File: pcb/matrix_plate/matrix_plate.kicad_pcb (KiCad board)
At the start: 2 copper layers, 269.2 x 122.9 mm, 73 parts

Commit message: Continue re-routing matrix plate to move diodes to front.
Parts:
- moved R_R_A1 7.63 mm to (256.0, 42.0)
- moved R_R_A2 7.63 mm to (256.0, 44.5)
- moved R_L_SCL_1 6.52 mm to (46.0, 37.0)
- moved R_R_SCL_1 6.52 mm to (260.5, 39.5), turned to 0 degrees
- moved R_R_SDA_1 6.52 mm to (260.5, 37.0), turned to 180 degrees
- moved R_L_A0 5.50 mm to (42.0, 44.5), turned to 0 degrees
- moved R_L_A1 5.50 mm to (42.0, 42.0), turned to 180 degrees
- moved R_L_A2 5.50 mm to (42.0, 39.5), turned to 180 degrees
- moved R_R_A0 4.27 mm to (256.0, 39.5)
- moved R_R_RST_1 4.27 mm to (256.0, 37.0)
- moved R_L_SDA_1 4.00 mm to (46.0, 39.5)
- moved R_L_RST_1 0.15 mm to (42.0, 37.0), turned to 180 degrees
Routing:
- net /Right/R3: track 50.9 -> 245.9 mm, vias 0 -> 1
- net /Right/CHG_STAT: track 0.00 -> 194.6 mm, vias 0 -> 2
- net /Left/SDA: track 0.00 -> 190.4 mm
- net /Left/SCL: track 0.00 -> 189.6 mm
- net /Right/C5: track 1.60 -> 186.2 mm, vias 1 -> 0
- net /Right/R2: track 61.0 -> 230.2 mm, vias 0 -> 1
- net /Right/R1: track 61.0 -> 225.8 mm, vias 0 -> 1
- net /Left/C5: track 39.9 -> 204.2 mm, vias 1 -> 0
- net /Right/C4: track 1.64 -> 143.8 mm, vias 1 -> 0
- net /Right/C3: track 1.52 -> 129.4 mm, vias 1 -> 0
- net /Left/C4: track 60.4 -> 164.9 mm, vias 1 -> 0
- net /Right/C2: track 1.62 -> 99.4 mm, vias 1 -> 0
- net /Left/R3: track 144.2 -> 240.4 mm, vias 0 -> 1
- net /Right/C0: track 1.00 -> 95.4 mm, vias 1 -> 0
- net /Right/R0: track 51.3 -> 139.0 mm, vias 0 -> 1
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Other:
- outline, holes or cut-outs redrawn

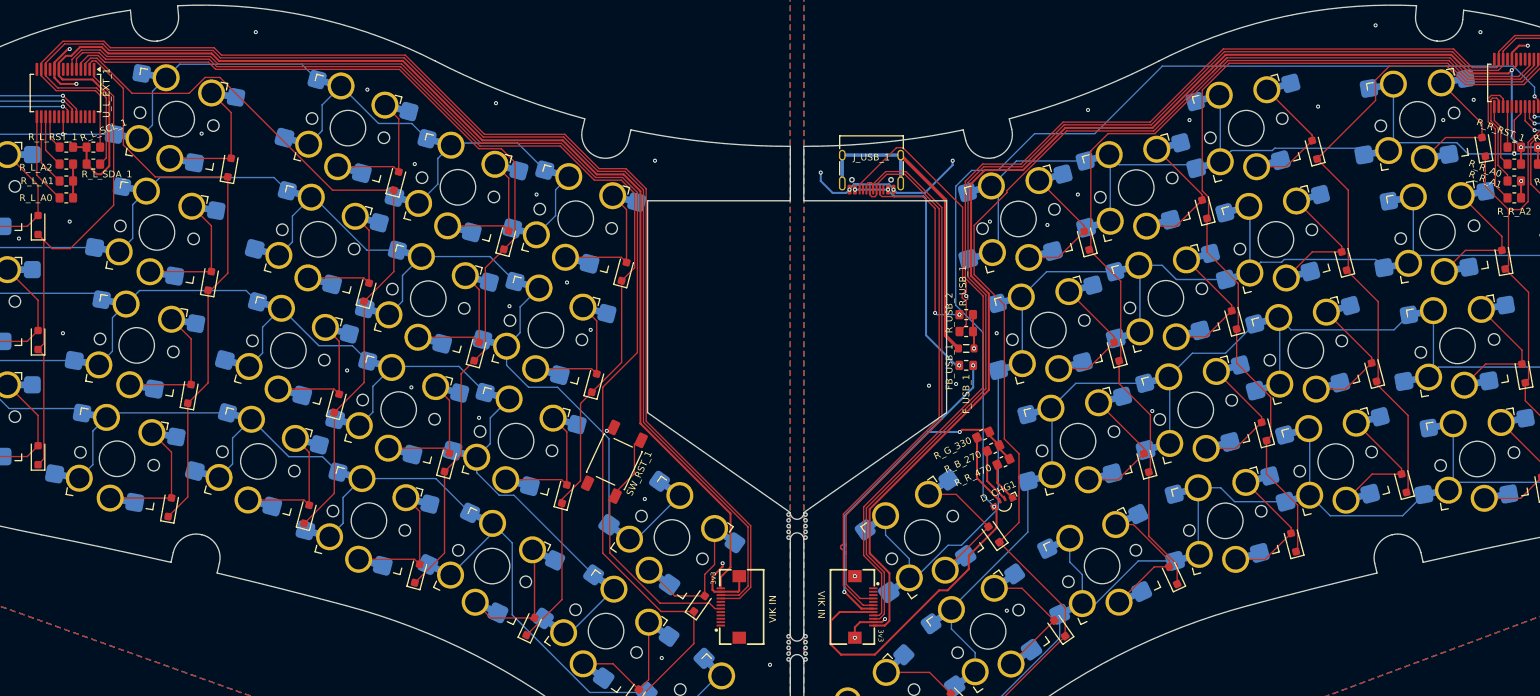
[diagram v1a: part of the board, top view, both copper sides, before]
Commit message: Finish re-routing matrix PCB.
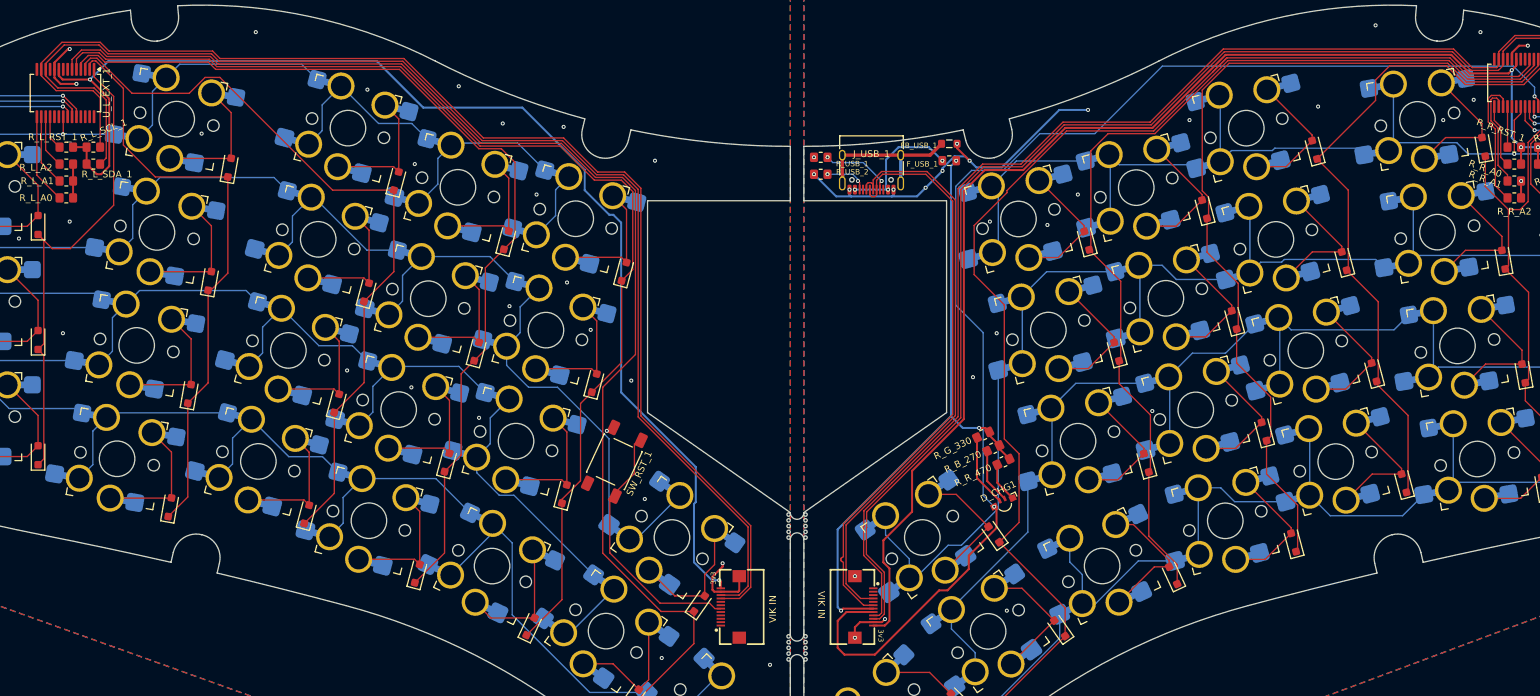
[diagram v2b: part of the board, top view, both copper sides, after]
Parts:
- moved R_USB_1 31.7 mm to (153.5, 38.5), turned to 180 degrees
- moved R_USB_2 31.7 mm to (153.5, 41.0), turned to 180 degrees
- moved FB_USB_1 30.4 mm to (172.5, 36.5)
- moved F_USB_1 30.4 mm to (172.5, 39.0)
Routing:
- net Net-(J_USB_1-CC2): track 41.7 -> 6.43 mm, vias 0 -> 2
- net /Right/VUSB: track 61.2 -> 90.7 mm
- net /Right/SH: track 49.1 -> 23.7 mm
- net /Right/GND: track 42.8 -> 66.4 mm, vias 32 -> 33
- net /Right/VUSB_RAW: track 38.1 -> 19.4 mm
- net Net-(J_USB_1-CC1): track 28.9 -> 10.8 mm
- net /Left/VDD: track 190.4 -> 181.0 mm, vias 0 -> 2
- net /Right/VDD: track 187.4 -> 183.5 mm
- net /Right/D+: track 83.1 -> 86.9 mm
- net /Right/D-: track 83.1 -> 86.9 mm
- net /Right/SDA: track 190.3 -> 188.2 mm
- net /Right/SCL: track 193.6 -> 191.4 mm
- net /Right/CHG_STAT: track 194.6 -> 193.3 mm
- net /Left/SDA: track 190.4 -> 189.6 mm
- net /Left/SCL: track 189.6 -> 188.9 mm
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
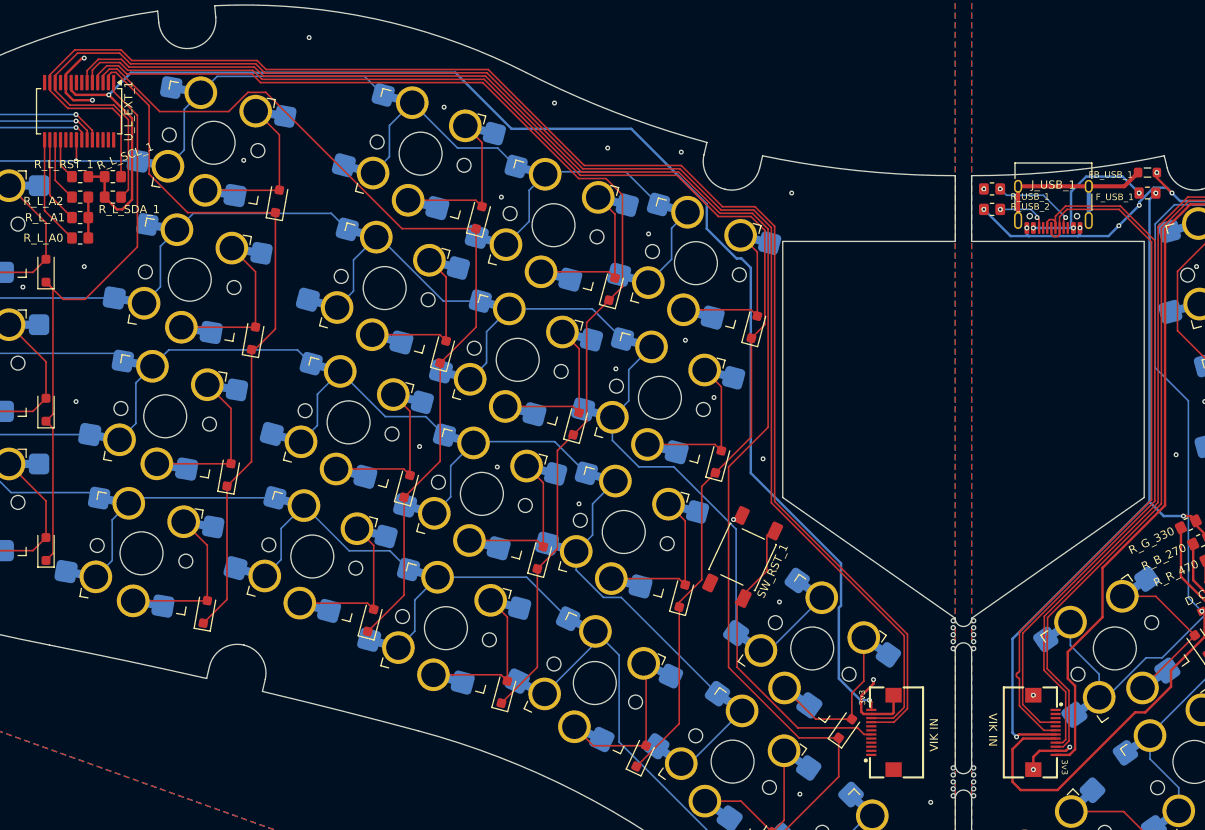
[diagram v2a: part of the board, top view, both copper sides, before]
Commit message: Update KiCAD projects to use new library locations.
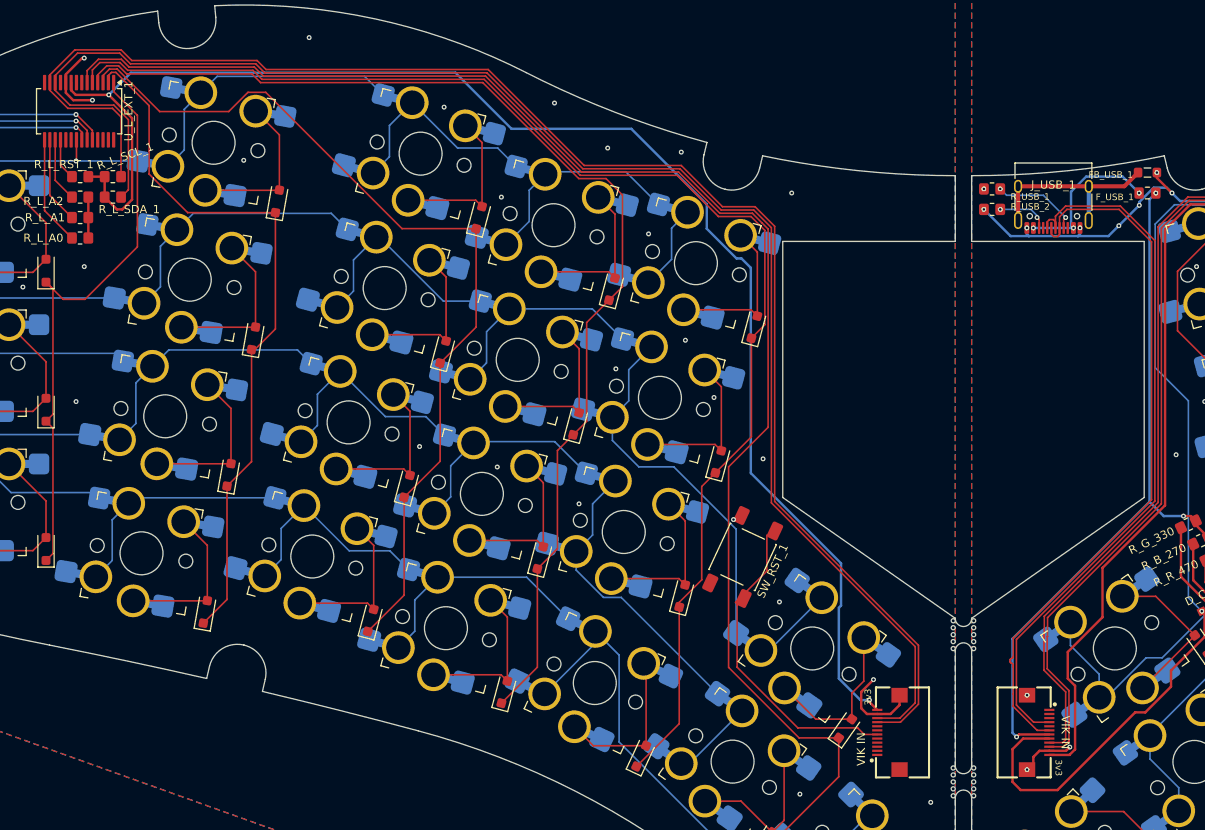
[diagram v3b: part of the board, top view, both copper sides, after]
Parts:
- J_L_VIK_1, J_R_VIK_1: footprint vik:vik-module-connector-horizontal -> footprints:vik-module-connector-horizontal
- S_L_00, S_L_01, S_L_02, S_L_03, S_L_04, S_L_10, S_L_11, S_L_12, S_L_13, S_L_14, S_L_15, S_L_20, S_L_21, S_L_22, S_L_23, S_L_24, S_L_25, S_L_31, S_L_32, S_L_33, S_L_34, S_L_35, S_R_00, S_R_01, S_R_02, S_R_03, S_R_04, S_R_10, S_R_11, S_R_12, S_R_13, S_R_14, S_R_15, S_R_20, S_R_21, S_R_22, S_R_23, S_R_24, S_R_25, S_R_31, S_R_32, S_R_33, S_R_34, S_R_35: footprint key-switches:SW_GLP_Kailh_Choc_V1V2_HotSwap_PTH -> footprints:SW_GLP_Kailh_Choc_V1V2_HotSwap_PTH
- moved J_R_VIK_1 0.77 mm to (158.5, 105.0)
- moved J_L_VIK_1 0.73 mm to (141.5, 105.0)
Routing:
- net /Left/SDA: track 189.6 -> 190.4 mm
- net /Left/SCL: track 188.9 -> 189.7 mm
- net /Right/SDA: track 188.2 -> 188.9 mm
- net /Right/VUSB: track 90.7 -> 90.0 mm
- net /Right/VDD: track 183.5 -> 184.3 mm
- net /Right/SCL: track 191.4 -> 192.2 mm
- net /Right/CHG_STAT: track 193.3 -> 192.6 mm
- net /Left/RST: track 38.4 -> 39.1 mm
